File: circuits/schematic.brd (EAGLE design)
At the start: 100 x 80 mm, 38 parts, among them IC1 MEGA8-P, IC2 MAX481CPA, J1 AVR_SPI_PRG_6PTH

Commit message: Circuit layout v1.
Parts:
- added R14, R15, R16, R17: (no value), SparkFun-Passives:AXIAL-0.4
- moved JP3 51.7 mm to (80.0, 49.5), turned to 90 degrees
- moved JP1 49.1 mm to (80.0, 26.7), turned to 90 degrees
- moved R2 38.4 mm to (61.0, 24.1)
- moved JP2 30.6 mm to (80.0, 38.1), turned to 90 degrees
- moved IC2 29.2 mm to (30.5, 59.7)
- moved R9 26.9 mm to (47.0, 24.1)
- moved J1 25.4 mm to (30.5, 33.0), turned to 270 degrees
- moved JP4 25.0 mm to (80.0, 61.0), turned to 90 degrees
- moved U$3 20.4 mm to (64.8, 34.3), turned to 180 degrees
- moved U$12 12.0 mm to (64.8, 53.3), turned to 180 degrees
- moved U$5 12.0 mm to (64.8, 40.6), turned to 180 degrees
- moved U$6 11.4 mm to (71.1, 25.4), turned to 180 degrees
- moved U$4 11.4 mm to (71.1, 38.1), turned to 180 degrees
- moved U$10 10.9 mm to (64.8, 47.0), turned to 180 degrees
- moved R13 10.2 mm to (47.0, 64.8)
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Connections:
- removed net N$14: IC1.16, R4.P$1
- removed net N$37: IC1.12, JP2.6
- removed net N$38: R11.P$2, U$12.2
- removed net N$44: IC1.27, R12.P$1
- removed net N$46: IC1.13, JP4.6
- removed net N$49: IC1.26, R11.P$1
- new net N$50: IC1.28, R16.P$1
- new net N$51: JP4.3, U$12.1
- new net N$52: JP4.5, U$13.1
- new net N$53: JP4.4, U$14.1
- new net N$54: IC1.17, J1.4, R3.P$1
- new net N$55: IC1.18, J1.1, R4.P$1
- net GND: now also J1.6, R13.P$2, R17.P$2, R2.P$2, R9.P$2, U$10.3, U$11.3, U$12.3, U$13.3, U$14.3, U$3.3, U$4.3, U$5.3, U$6.3, U$7.3, U$8.3, U$9.3; no longer JP1.1, JP1.2, JP2.1, JP2.2, JP3.1, JP3.2, JP4.1, JP4.2
- net N$10: now also JP1.4, U$8.1; no longer JP3.5, U$4.3
- net N$11: now also IC1.27, R15.P$1; no longer JP3.4, U$5.3
- net N$12: now also R5.P$1; no longer R2.P$1
- net N$13: now also R6.P$1; no longer R3.P$1
- net N$15: now also JP1.6, R2.P$1; no longer JP3.6
- net N$21: now also IC1.11, JP2.6, R9.P$1; no longer JP1.3, U$6.3
- net N$23: now also R3.P$2, U$3.2; no longer JP1.5, U$7.3
- net N$24: now also R4.P$2, U$4.2; no longer JP1.4, U$8.3
- net N$25: now also U$5.2; no longer U$9.2
- net N$26: now also IC1.19, J1.3, R8.P$1; no longer IC1.18, R6.P$1
- net N$27: now also IC1.16; no longer IC1.19
- net N$28: now also JP2.3, U$3.1; no longer R4.P$2, U$5.2
- net N$29: now also JP2.5, U$4.1; no longer IC1.11, JP1.6
- net N$3: now also IC1.26, R14.P$1; no longer R2.P$2, U$3.2
- net N$30: now also JP2.4, U$5.1; no longer R9.P$2, U$10.2
- net N$31: now also IC1.12, JP3.6, R13.P$1; no longer R10.P$2, U$11.2
- net N$32: now also R10.P$2, U$9.2; no longer JP2.3, U$9.3
- net N$33: now also R11.P$2, U$10.2; no longer JP2.5, U$10.3
- net N$34: now also R12.P$2, U$11.2; no longer JP2.4, U$11.3
- net N$35: now also R11.P$1; no longer R9.P$1
- net N$36: now also R12.P$1; no longer R10.P$1
- net N$39: now also JP3.3, U$9.1; no longer R12.P$2, U$13.2
- net N$40: now also JP3.5, U$10.1; no longer R13.P$2, U$14.2
- net N$41: now also JP3.4, U$11.1; no longer JP4.3, U$12.3
- net N$42: now also IC1.13, JP4.6, R17.P$1; no longer JP4.5, U$13.3
- net N$43: now also R14.P$2, U$12.2; no longer JP4.4, U$14.3
- net N$45: now also R15.P$2, U$13.2; no longer IC1.28, R13.P$1
- net N$47: now also R16.P$2, U$14.2; no longer IC1.17, R5.P$1
- net N$48: now also R10.P$1; no longer R8.P$1
- net N$6: now also JP1.3, U$6.1; no longer R3.P$2, U$4.2
- net N$9: now also JP1.5, U$7.1; no longer JP3.3, U$3.3
- net VCC: now also JP1.1, JP1.2, JP2.1, JP2.2, JP3.1, JP3.2, JP4.1, JP4.2; no longer U$10.1, U$11.1, U$12.1, U$13.1, U$14.1, U$3.1, U$4.1, U$5.1, U$6.1, U$7.1, U$8.1, U$9.1

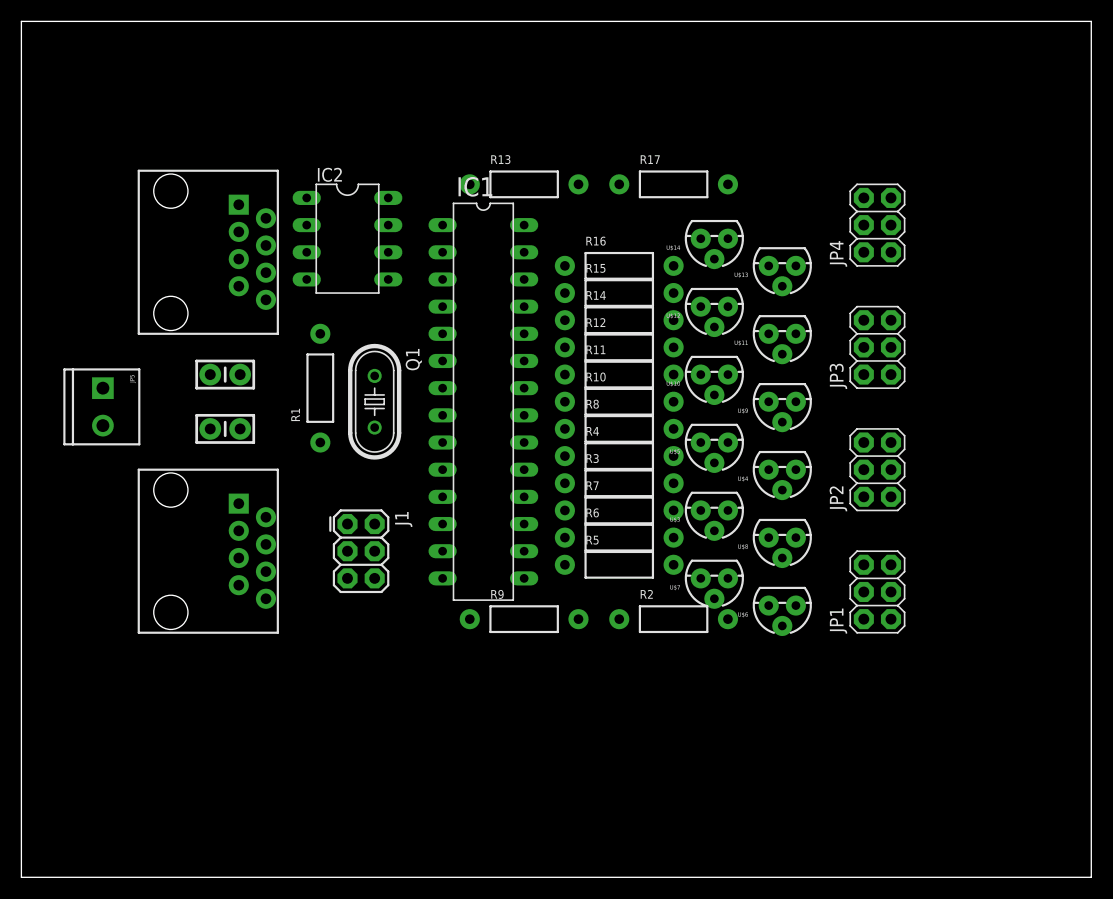
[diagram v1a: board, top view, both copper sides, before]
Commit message: Right side layout.
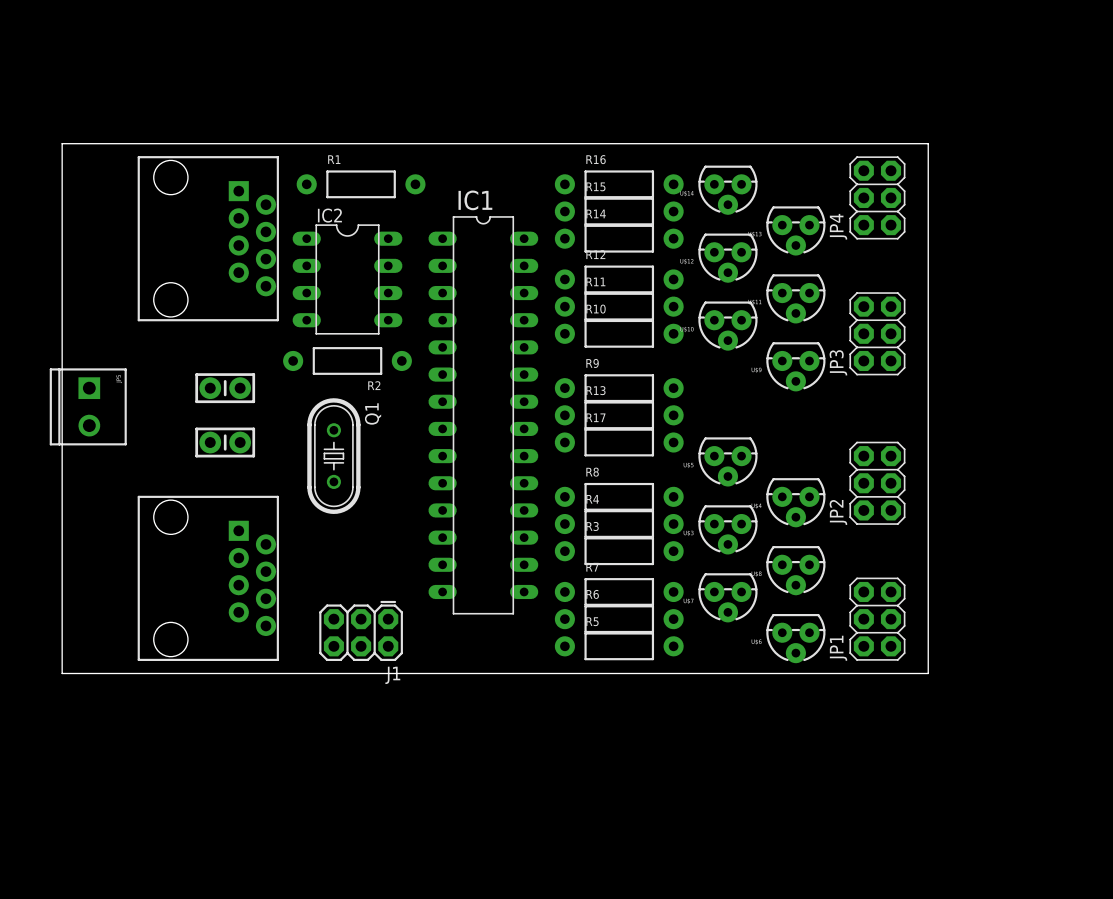
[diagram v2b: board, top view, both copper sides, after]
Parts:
- moved R2 38.9 mm to (30.5, 48.3), turned to 180 degrees
- moved R17 24.7 mm to (55.9, 40.6)
- moved R9 23.3 mm to (55.9, 45.7)
- moved R13 23.3 mm to (55.9, 43.2)
- moved R1 19.4 mm to (31.8, 64.8), turned to 0 degrees
- moved J1 9.67 mm to (34.3, 24.1), turned to 180 degrees
- moved R5 7.62 mm to (55.9, 21.6)
- moved R6 7.62 mm to (55.9, 24.1)
- moved R14 7.62 mm to (55.9, 59.7)
- moved R15 7.62 mm to (55.9, 62.2)
- moved R16 7.62 mm to (55.9, 64.8)
- moved R7 7.62 mm to (55.9, 26.7)
- moved Q1 6.35 mm to (29.2, 39.4)
- moved R11 6.35 mm to (55.9, 53.3)
- moved R12 6.35 mm to (55.9, 55.9)
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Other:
- board size 100 x 80 mm -> 81 x 49.5 mm

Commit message: Autorouted, 50 mil, no vias.
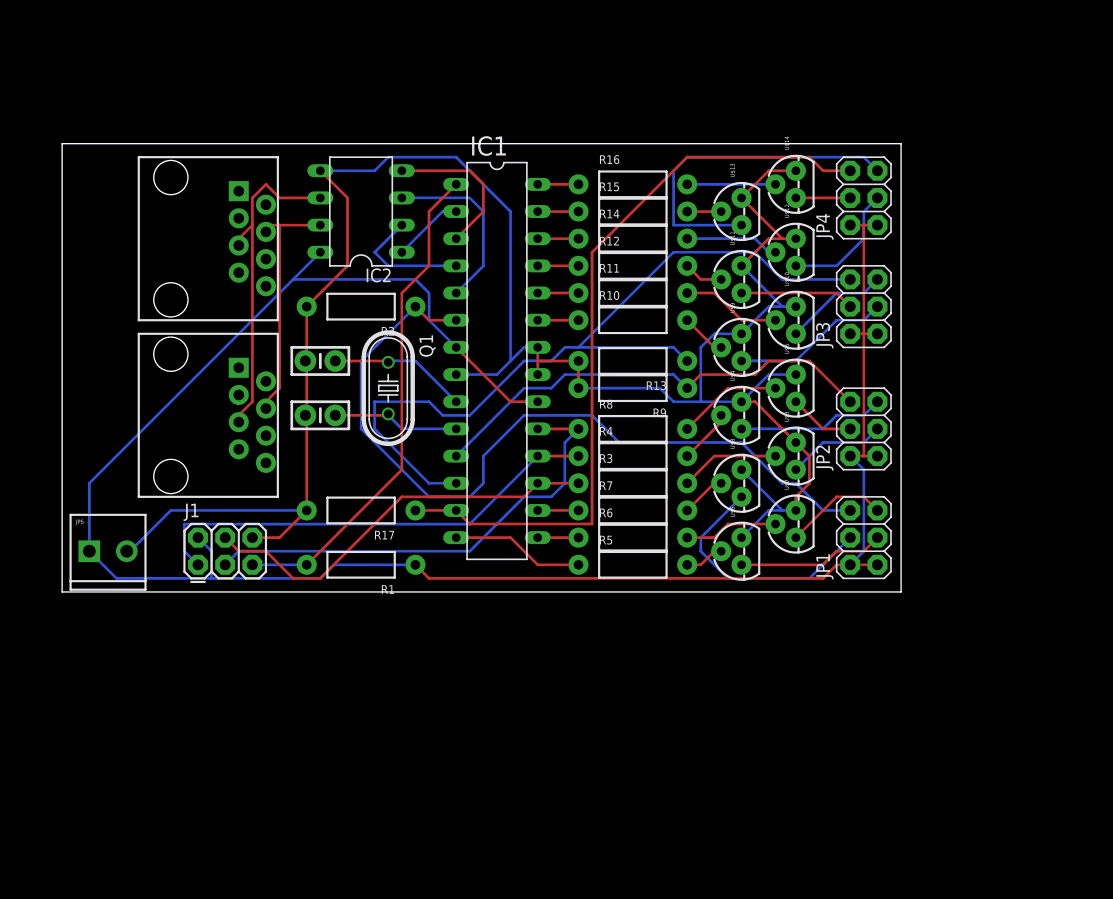
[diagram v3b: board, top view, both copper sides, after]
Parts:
- moved R1 35.6 mm to (31.8, 29.2), turned to 180 degrees
- moved R17 25.0 mm to (31.8, 34.3), turned to 180 degrees
- moved J1 18.5 mm to (16.5, 29.2), turned to 0 degrees
- moved JP5 15.2 mm to (6.35, 30.5), turned to 0 degrees
- moved U$2 15.2 mm to (14.0, 43.2)
- moved C1 9.25 mm to (27.9, 43.2)
- moved C2 9.25 mm to (27.9, 48.3)
- moved U$6 9.16 mm to (67.3, 30.5), turned to 90 degrees
- moved U$4 9.16 mm to (67.3, 43.2), turned to 90 degrees
- moved U$8 9.16 mm to (67.3, 36.8), turned to 90 degrees
- moved U$5 8.98 mm to (72.4, 45.7), turned to 90 degrees
- moved U$7 8.98 mm to (72.4, 33.0), turned to 90 degrees
- moved U$3 8.98 mm to (72.4, 39.4), turned to 90 degrees
- moved Q1 8.13 mm to (34.3, 45.7)
- moved JP1 7.73 mm to (78.7, 31.8)
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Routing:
- net GND: track 0.00 -> 197.2 mm
- net VCC: track 0.00 -> 187.0 mm
- net N$31: track 0.00 -> 75.3 mm
- net N$15: track 0.00 -> 74.5 mm
- net N$42: track 0.00 -> 70.8 mm
- net N$18: track 0.00 -> 46.4 mm
- net N$26: track 0.00 -> 44.3 mm
- net N$55: track 0.00 -> 43.8 mm
- net N$21: track 0.00 -> 43.1 mm
- net N$54: track 0.00 -> 38.3 mm
- net N$52: track 0.00 -> 31.5 mm
- net N$2: track 0.00 -> 31.3 mm
- net N$1: track 0.00 -> 23.4 mm
- net N$10: track 0.00 -> 23.3 mm
- net N$16: track 0.00 -> 16.8 mm
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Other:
- board size 81 x 49.5 mm -> 78.4 x 41.9 mm

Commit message: Start of board with custom vcc/gnd lines.
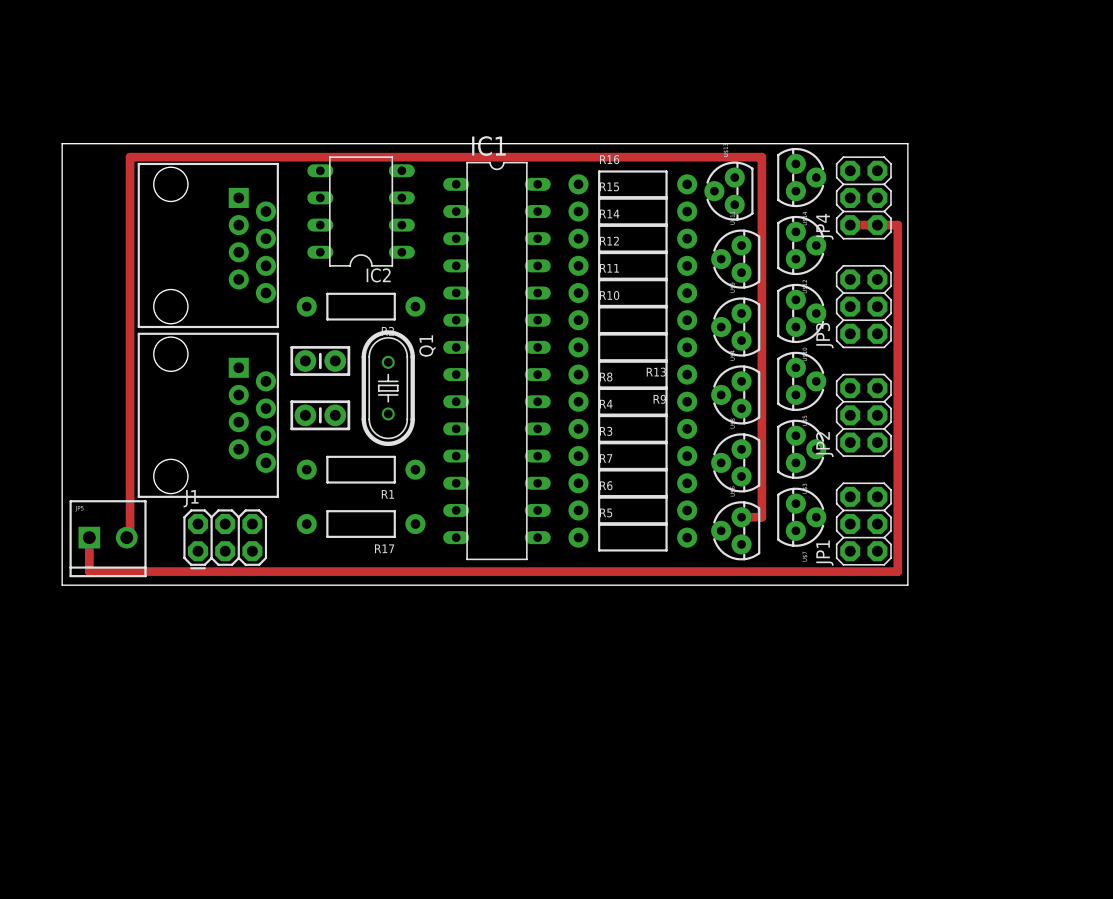
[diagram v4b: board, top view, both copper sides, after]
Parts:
- moved R1 8.89 mm to (31.8, 38.1)
- moved R8 2.54 mm to (57.1, 44.5)
- moved R3 2.54 mm to (57.1, 39.4)
- moved R4 2.54 mm to (57.1, 41.9)
- moved R5 2.54 mm to (57.1, 31.8)
- moved R6 2.54 mm to (57.1, 34.3)
- moved R7 2.54 mm to (57.1, 36.8)
- moved U$13 2.01 mm to (66.7, 64.1)
- moved U$4 1.91 mm to (67.3, 45.1)
- moved U$8 1.91 mm to (67.3, 38.7)
- moved U$9 1.91 mm to (67.3, 51.4)
- moved U$6 1.90 mm to (67.3, 32.4)
- moved U$11 1.90 mm to (67.3, 57.8)
- moved JP1 1.27 mm to (78.7, 33.0)
- moved JP2 1.27 mm to (78.7, 43.2)
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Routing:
- net N$31: track 75.3 -> 0.00 mm
- net N$15: track 74.5 -> 0.00 mm
- net VCC: track 187.0 -> 115.6 mm
- net N$42: track 70.8 -> 0.00 mm
- net GND: track 197.2 -> 130.5 mm
- net N$18: track 46.4 -> 0.00 mm
- net N$26: track 44.3 -> 0.00 mm
- net N$55: track 43.8 -> 0.00 mm
- net N$21: track 43.1 -> 0.00 mm
- net N$54: track 38.3 -> 0.00 mm
- net N$52: track 31.5 -> 0.00 mm
- net N$2: track 31.3 -> 0.00 mm
- net N$1: track 23.4 -> 0.00 mm
- net N$10: track 23.3 -> 0.00 mm
- net N$16: track 16.8 -> 0.00 mm
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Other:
- board size 78.4 x 41.9 mm -> 79 x 41.3 mm

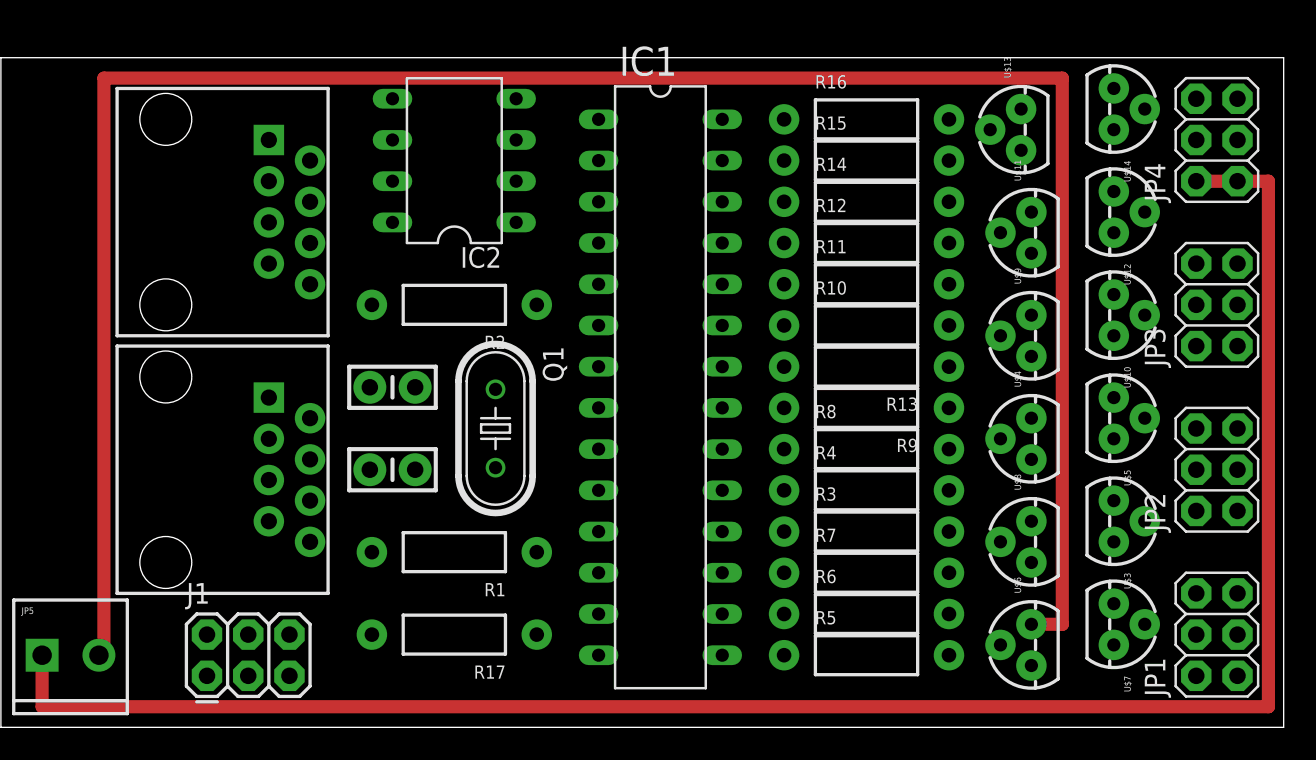
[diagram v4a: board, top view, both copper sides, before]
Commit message: Inverted switch order.
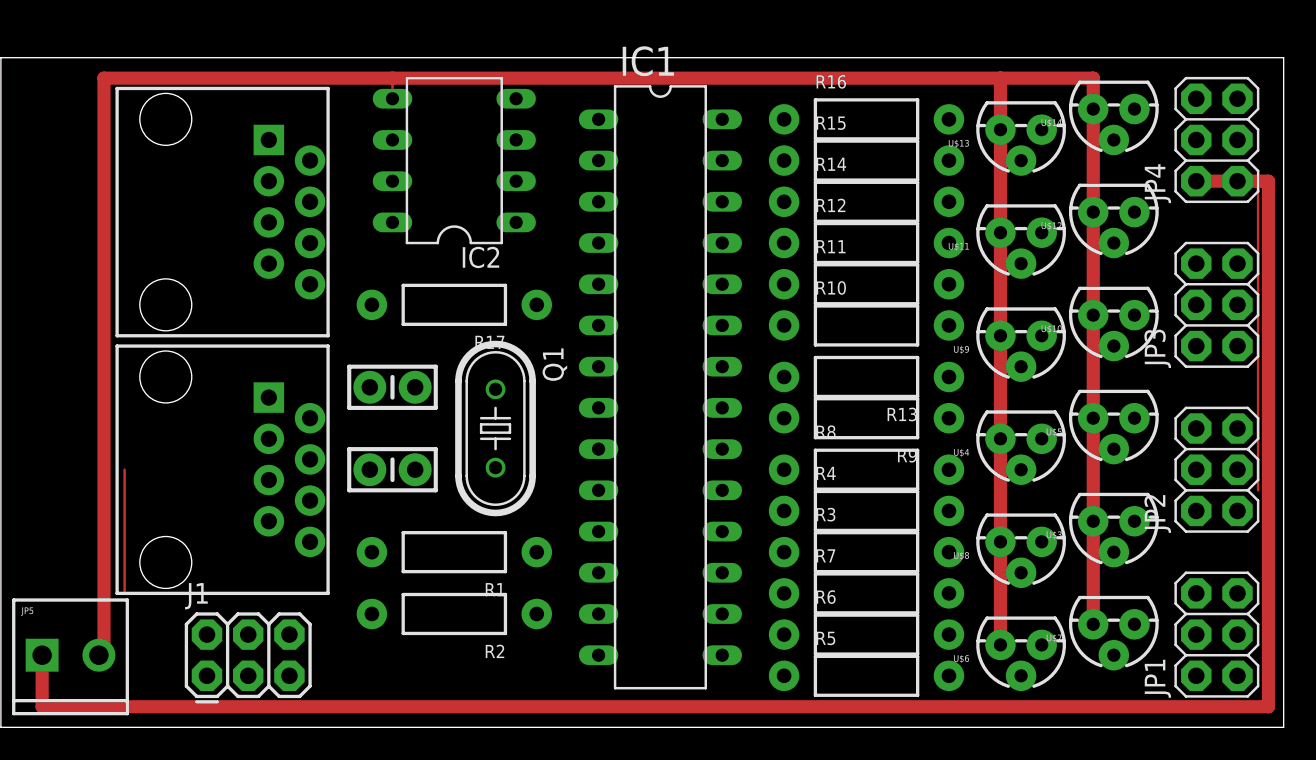
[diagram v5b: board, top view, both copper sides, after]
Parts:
- moved R17 20.3 mm to (31.8, 53.3)
- moved R2 19.1 mm to (31.8, 34.3)
- moved R8 1.27 mm to (57.1, 43.2)
- moved R5 1.27 mm to (57.1, 30.5)
- moved R3 1.27 mm to (57.1, 38.1)
- moved R4 1.27 mm to (57.1, 40.6)
- moved R6 1.27 mm to (57.1, 33.0)
- moved R7 1.27 mm to (57.1, 35.6)
- moved R9 0.64 mm to (57.1, 46.4)
- moved U$11 0.64 mm to (66.7, 57.8), turned to 180 degrees
- moved U$4 0.64 mm to (66.7, 45.1), turned to 180 degrees
- moved U$6 0.64 mm to (66.7, 32.4), turned to 180 degrees
- moved U$8 0.64 mm to (66.7, 38.7), turned to 180 degrees
- moved U$9 0.64 mm to (66.7, 51.4), turned to 180 degrees
- moved R13 0.63 mm to (57.1, 48.9)
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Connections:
- removed net N$15: IC1.6, JP1.6, R2.P$1
- new net N$14: IC1.13, JP1.6, R2.P$1
- net N$21: now also IC1.12; no longer IC1.11
- net N$31: now also IC1.11; no longer IC1.12
- net N$42: now also IC1.6; no longer IC1.13
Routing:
- net GND: track 130.5 -> 166.7 mm
- net VCC: track 115.6 -> 134.6 mm
- net N$55: track 0.00 -> 7.62 mm
- net N$18: track 0.00 -> 3.81 mm

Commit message: Self routed version.
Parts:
- moved R13 27.6 mm to (31.8, 38.1)
- moved R9 27.6 mm to (31.8, 35.6)
- moved U$6 14.1 mm to (80.6, 30.5), turned to 90 degrees
- moved U$9 14.0 mm to (80.6, 52.1), turned to 90 degrees
- moved U$8 11.2 mm to (74.3, 30.5), turned to 90 degrees
- moved JP1 9.67 mm to (87.6, 29.2), turned to 270 degrees
- moved U$11 9.53 mm to (74.3, 52.1), turned to 90 degrees
- moved JP2 9.25 mm to (87.6, 40.6), turned to 270 degrees
- moved JP3 8.98 mm to (87.6, 52.1), turned to 270 degrees
- moved R1 8.91 mm to (31.1, 29.2), turned to 0 degrees
- moved JP4 8.89 mm to (87.6, 63.5), turned to 270 degrees
- moved U$12 8.84 mm to (80.6, 62.2), turned to 90 degrees
- moved U$3 8.28 mm to (80.6, 40.6), turned to 90 degrees
- moved U$5 6.02 mm to (74.3, 40.6), turned to 90 degrees
- moved U$7 5.46 mm to (67.9, 30.5), turned to 90 degrees
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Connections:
- net GND: now also JP5.1; no longer JP5.2
- net VCC: now also JP5.2; no longer JP5.1
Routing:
- net VCC: track 134.6 -> 239.2 mm
- net N$18: track 3.81 -> 82.3 mm
- net N$31: track 0.00 -> 63.4 mm
- net N$14: track 0.00 -> 62.3 mm
- net N$42: track 0.00 -> 57.8 mm
- net GND: track 166.7 -> 221.7 mm
- net N$21: track 0.00 -> 53.9 mm
- net N$54: track 0.00 -> 43.0 mm
- net N$26: track 0.00 -> 40.6 mm
- net N$2: track 0.00 -> 34.9 mm
- net N$55: track 7.62 -> 37.0 mm
- net N$1: track 0.00 -> 22.8 mm
- net N$52: track 0.00 -> 20.6 mm
- net N$9: track 0.00 -> 19.5 mm
- net N$40: track 0.00 -> 19.5 mm
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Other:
- board size 79 x 41.3 mm -> 87.9 x 43.8 mm
